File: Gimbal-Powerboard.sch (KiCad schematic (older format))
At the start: 117 parts

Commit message: Replaced legacy LaunchXL headers with new LaunchXL header device in schematic
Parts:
- removed U?: TIVA_Header_Pins, symbol TIVA_Header_Pins
- added U3: LAUNCHXL-F28069M_Launchpad_J1, MRDT_Shields:LAUNCHXL-F28069M_Launchpad_Programmer_Side, symbol LAUNCHXL-F28069M_Launchpad_J1
- gave numbers to parts that had none: 116
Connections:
- net ASENSE: now also U3.A_B1 (J3_24)
- net BSENSE: now also U3.A_A2 (J3_25)
- net CSENSE: now also U3.A_B2 (J3_26)
- net DC_CAL: now also U3.P_51 (J2_12)
- net DE: now also U3.P_13 (J4_34)
- net EN_GATE: now also U3.P_50 (J2_13)
- net GND: now also U3.GND (J3_22)
- net INH_A: now also U3.P_0 (J4_40)
- net INH_B: now also U3.P_2 (J4_38)
- net INH_C: now also U3.P_4 (J4_36)
- net INL_A: now also U3.P_1 (J4_39)
- net INL_B: now also U3.P_3 (J4_37)
- net INL_C: now also U3.P_5 (J4_35)
- net NFAULT: now also U3.P_33 (J1_9)
- net NOCTW: now also U3.P_32 (J1_10)
- net NSCS: now also U3.P_19 (J2_19)
- net PVDDSENSE: now also U3.A_A7 (J3_23)
- net PWM_IN: now also U3.DAC2 (J4_31)
- net SCLK: now also U3.P_18 (J1_7)
- net SDI: now also U3.P_16 (J2_15)
- net SDO: now also U3.P_17 (J2_14)
- net SO1: now also U3.A_A0 (J3_27)
- net SO2: now also U3.A_B0 (J3_28)
- net UART_RX: now also U3.P_28 (J1_3)
- net UART_TX: now also U3.P_29 (J1_4)
- net VCC: now also U3.+3V3 (J1_1)

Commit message: Github Fix Commit
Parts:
- removed C7: C, symbol C
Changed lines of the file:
@@
 EESchema Schematic File Version 2
-LIBS:Gimbal-Powerboard-rescue
 LIBS:power
 LIBS:device
@@
 LIBS:contrib
 LIBS:valves
-LIBS:MRDT-Actives
-LIBS:MRDT-Connectors
-LIBS:MRDT-Devices
-LIBS:MRDT-Drill_Holes
-LIBS:MRDT-Headers
-LIBS:MRDT-ICs
-LIBS:MRDT-Passives
-LIBS:MRDT-Shields
-LIBS:MRDT-Silkscreens
-LIBS:MRDT-Switches
 LIBS:Gimbal-Powerboard-cache
 EELAYER 25 0
@@
 F 2 "" H 5288 4900 50  0001 C CNN
 F 3 "" H 5250 5050 50  0001 C CNN
-	1    5250 5050
-	1    0    0    -1
-$EndComp
-$Comp
-L C C7
-U 1 1 5A7F8D38
-P 5250 5050
-F 0 "C7" H 5275 5150 50  0000 L CNN
-F 1 "C" H 5275 4950 50  0000 L CNN
-F 2 "" H 5288 4900 50  0001 C CNN
-F 3 "" H 5250 5050 50  0001 C CNN

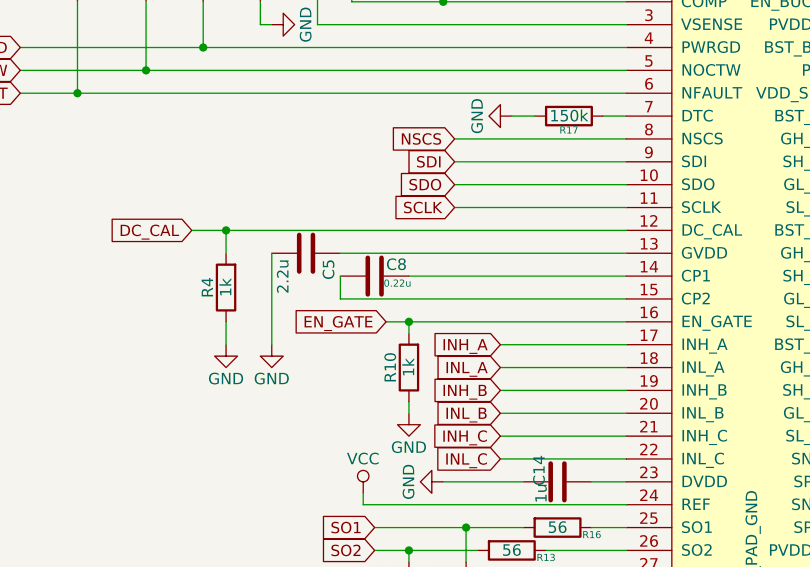
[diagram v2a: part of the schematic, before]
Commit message: Started device/package pairing
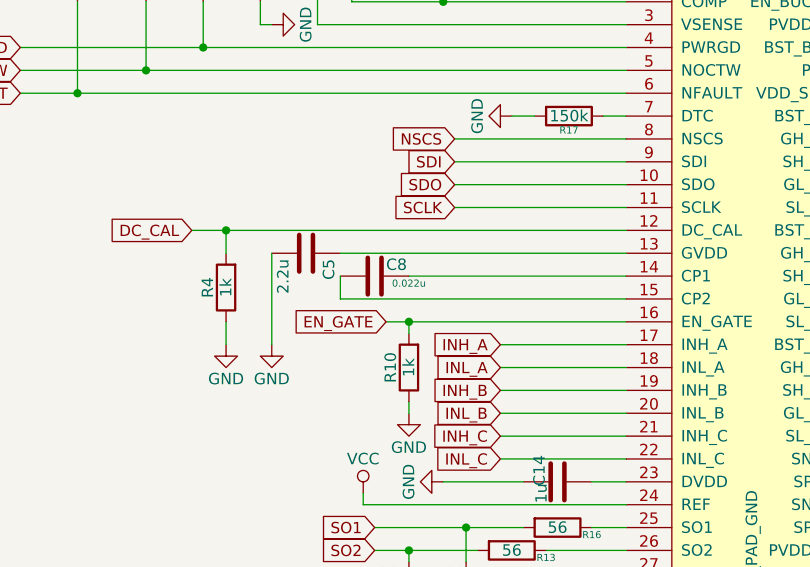
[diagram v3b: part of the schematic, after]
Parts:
- C1, C2: footprint (none) -> Capacitors_THT:CP_Radial_D12.5mm_P5.00mm
- C10, C11, C12, C13, C14, C15, C16, C17, C18, C20, C21, C23, C24, C25, C26, C27, C28, C3, C32, C33, C34, C35, C36, C4, C41, C42, C43, C6, C9: footprint (none) -> Capacitors_SMD:C_0805_HandSoldering
- C19, C22, C29, C30, C31, C5: footprint (none) -> Capacitors_SMD:C_1206_HandSoldering
- C8: value 0.22u -> 0.022u; footprint (none) -> Capacitors_SMD:C_0805_HandSoldering
- D1, D2, D3, D4: footprint (none) -> LEDs:LED_1206_HandSoldering
- D10, D11, D5, D6, D7, D8, D9: footprint (none) -> Diodes_SMD:D_SOD-323_HandSoldering

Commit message: Paired devices and packages for all components of schematic except MAX3232
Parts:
- C37: footprint (none) -> MRDT-Connectors:Anderson_2_Horisontal_Side-by-Side
- C38, C39, C40: footprint (none) -> MRDT-Connectors:Anderson_1_Horisontal
- L1: footprint (none) -> MRDT-Passives:DR74-330-R
- Q1, Q2: footprint (none) -> Diodes_SMD:D_SOT-23_ANK
- Q3, Q4, Q5, Q6, Q7, Q8: footprint (none) -> MRDT-Actives:Rohm_R6020ENJ_N-Channel_MOSFET
- R1, R10, R11, R12, R13, R14, R15, R16, R17, R18, R19, R2, R20, R21, R22, R23, R24, R25, R28, R29, R3, R30, R31, R32, R33, R4, R5, R6, R7, R8, R9: footprint (none) -> Resistors_SMD:R_0805_HandSoldering
- R26, R27: footprint (none) -> Resistors_SMD:R_1206_HandSoldering
- U1: footprint (none) -> MRDT-ICs:DRV8301
- U2: footprint (none) -> MRDT-ICs:NUP4201MR6
- U5: footprint (none) -> MRDT-Connectors:MOLEX_SL_3
- U6: footprint (none) -> MRDT-Connectors:MOLEX_SL_5

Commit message: Finished pairing devices with packages and generated netlist
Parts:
- TP1, TP10, TP11, TP12, TP13, TP14, TP15, TP2, TP3, TP4, TP5, TP6, TP7, TP8, TP9: footprint (none) -> Wire_Pads:SolderWirePad_single_1mmDrill
- U3: footprint MRDT_Shields:LAUNCHXL-F28069M_Launchpad_Programmer_Side -> MRDT_Shields:LAUNCHXL-F28069M_Launchpad_J1
- U4: footprint (none) -> MRDT_ICs:SOIC-16_3.9x9.9mm_Pitch1.27mm
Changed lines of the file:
@@
 F 0 "TP1" H 3800 3050 50  0000 C BNN
 F 1 "TEST" H 3800 3000 50  0000 C CNN
-F 2 "" H 3800 2750 50  0001 C CNN
+F 2 "Wire_Pads:SolderWirePad_single_1mmDrill" H 3800 2750 50  0001 C CNN
 F 3 "" H 3800 2750 50  0001 C CNN
 	1    3800 2750
@@
 F 0 "TP2" H 4350 5100 50  0000 C BNN
 F 1 "TEST" H 4350 5050 50  0000 C CNN
-F 2 "" H 4350 4800 50  0001 C CNN
+F 2 "Wire_Pads:SolderWirePad_single_1mmDrill" H 4350 4800 50  0001 C CNN
 F 3 "" H 4350 4800 50  0001 C CNN
 	1    4350 4800
@@
 F 0 "TP7" H 11950 3000 50  0000 C BNN
 F 1 "TEST" H 11950 2950 50  0000 C CNN
-F 2 "" H 11950 2700 50  0001 C CNN
+F 2 "Wire_Pads:SolderWirePad_single_1mmDrill" H 11950 2700 50  0001 C CNN
 F 3 "" H 11950 2700 50  0001 C CNN
 	1    11950 2700
@@
 F 0 "TP10" H 12950 3600 50  0000 C BNN
 F 1 "TEST" H 12950 3550 50  0000 C CNN
-F 2 "" H 12950 3300 50  0001 C CNN
+F 2 "Wire_Pads:SolderWirePad_single_1mmDrill" H 12950 3300 50  0001 C CNN
 F 3 "" H 12950 3300 50  0001 C CNN
 	1    12950 3300
@@
 F 0 "TP4" H 11800 3950 50  0000 C BNN
 F 1 "TEST" H 11800 3900 50  0000 C CNN
-F 2 "" H 11800 3650 50  0001 C CNN
+F 2 "Wire_Pads:SolderWirePad_single_1mmDrill" H 11800 3650 50  0001 C CNN
 F 3 "" H 11800 3650 50  0001 C CNN
 	1    11800 3650
@@
 F 0 "TP8" H 11950 6200 50  0000 C BNN
 F 1 "TEST" H 11950 6150 50  0000 C CNN
-F 2 "" H 11950 5900 50  0001 C CNN
+F 2 "Wire_Pads:SolderWirePad_single_1mmDrill" H 11950 5900 50  0001 C CNN
 F 3 "" H 11950 5900 50  0001 C CNN
 	1    11950 5900
@@
 F 0 "TP11" H 12950 6800 50  0000 C BNN
 F 1 "TEST" H 12950 6750 50  0000 C CNN
-F 2 "" H 12950 6500 50  0001 C CNN
+F 2 "Wire_Pads:SolderWirePad_single_1mmDrill" H 12950 6500 50  0001 C CNN
 F 3 "" H 12950 6500 50  0001 C CNN
 	1    12950 6500
@@
 F 0 "TP5" H 11800 7150 50  0000 C BNN
 F 1 "TEST" H 11800 7100 50  0000 C CNN
-F 2 "" H 11800 6850 50  0001 C CNN
+F 2 "Wire_Pads:SolderWirePad_single_1mmDrill" H 11800 6850 50  0001 C CNN
 F 3 "" H 11800 6850 50  0001 C CNN
 	1    11800 6850
@@
 F 0 "TP6" H 11900 9400 50  0000 C BNN
 F 1 "TEST" H 11900 9350 50  0000 C CNN
-F 2 "" H 11900 9100 50  0001 C CNN
+F 2 "Wire_Pads:SolderWirePad_single_1mmDrill" H 11900 9100 50  0001 C CNN
 F 3 "" H 11900 9100 50  0001 C CNN
 	1    11900 9100
@@
 F 0 "TP9" H 12900 10000 50  0000 C BNN
 F 1 "TEST" H 12900 9950 50  0000 C CNN
-F 2 "" H 12900 9700 50  0001 C CNN
+F 2 "Wire_Pads:SolderWirePad_single_1mmDrill" H 12900 9700 50  0001 C CNN
 F 3 "" H 12900 9700 50  0001 C CNN
 	1    12900 9700
@@
 F 0 "TP3" H 11750 10350 50  0000 C BNN
 F 1 "TEST" H 11750 10300 50  0000 C CNN
-F 2 "" H 11750 10050 50  0001 C CNN
+F 2 "Wire_Pads:SolderWirePad_single_1mmDrill" H 11750 10050 50  0001 C CNN
 F 3 "" H 11750 10050 50  0001 C CNN
 	1    11750 10050
@@
 F 0 "U4" H 17050 11025 50  0000 R CNN
 F 1 "MAX3232" H 17050 10950 50  0000 R CNN
-F 2 "" H 17200 8850 50  0001 L CNN
+F 2 "MRDT_ICs:SOIC-16_3.9x9.9mm_Pitch1.27mm" H 17200 8850 50  0001 L CNN
 F 3 "" H 17150 10000 50  0001 C CNN
 	1    17150 9900
@@
 F 0 "TP12" H 18050 5450 50  0000 C BNN
 F 1 "TEST" H 18050 5400 50  0000 C CNN
-F 2 "" H 18050 5150 50  0001 C CNN
+F 2 "Wire_Pads:SolderWirePad_single_1mmDrill" H 18050 5150 50  0001 C CNN
 F 3 "" H 18050 5150 50  0001 C CNN
 	1    18050 5150
@@
 F 0 "TP13" H 18200 5450 50  0000 C BNN
 F 1 "TEST" H 18200 5400 50  0000 C CNN
-F 2 "" H 18200 5150 50  0001 C CNN
+F 2 "Wire_Pads:SolderWirePad_single_1mmDrill" H 18200 5150 50  0001 C CNN
 F 3 "" H 18200 5150 50  0001 C CNN
 	1    18200 5150
@@
 F 0 "TP14" H 18350 5450 50  0000 C BNN
 F 1 "TEST" H 18350 5400 50  0000 C CNN
-F 2 "" H 18350 5150 50  0001 C CNN
+F 2 "Wire_Pads:SolderWirePad_single_1mmDrill" H 18350 5150 50  0001 C CNN
 F 3 "" H 18350 5150 50  0001 C CNN
 	1    18350 5150
@@
 F 0 "TP15" H 18500 5450 50  0000 C BNN
 F 1 "TEST" H 18500 5400 50  0000 C CNN
-F 2 "" H 18500 5150 50  0001 C CNN
+F 2 "Wire_Pads:SolderWirePad_single_1mmDrill" H 18500 5150 50  0001 C CNN
 F 3 "" H 18500 5150 50  0001 C CNN
 	1    18500 5150
@@
 F 0 "U3" H 16050 6500 60  0001 C CNN
 F 1 "LAUNCHXL-F28069M_Launchpad_J1" H 16200 7850 60  0000 C CNN
-F 2 "MRDT_Shields:LAUNCHXL-F28069M_Launchpad_Programmer_Side" H 15950 6550 60  0001 C CNN
+F 2 "MRDT_Shields:LAUNCHXL-F28069M_Launchpad_J1" H 15950 6550 60  0001 C CNN
 F 3 "" H 15950 6550 60  0001 C CNN
 	1    15950 5300

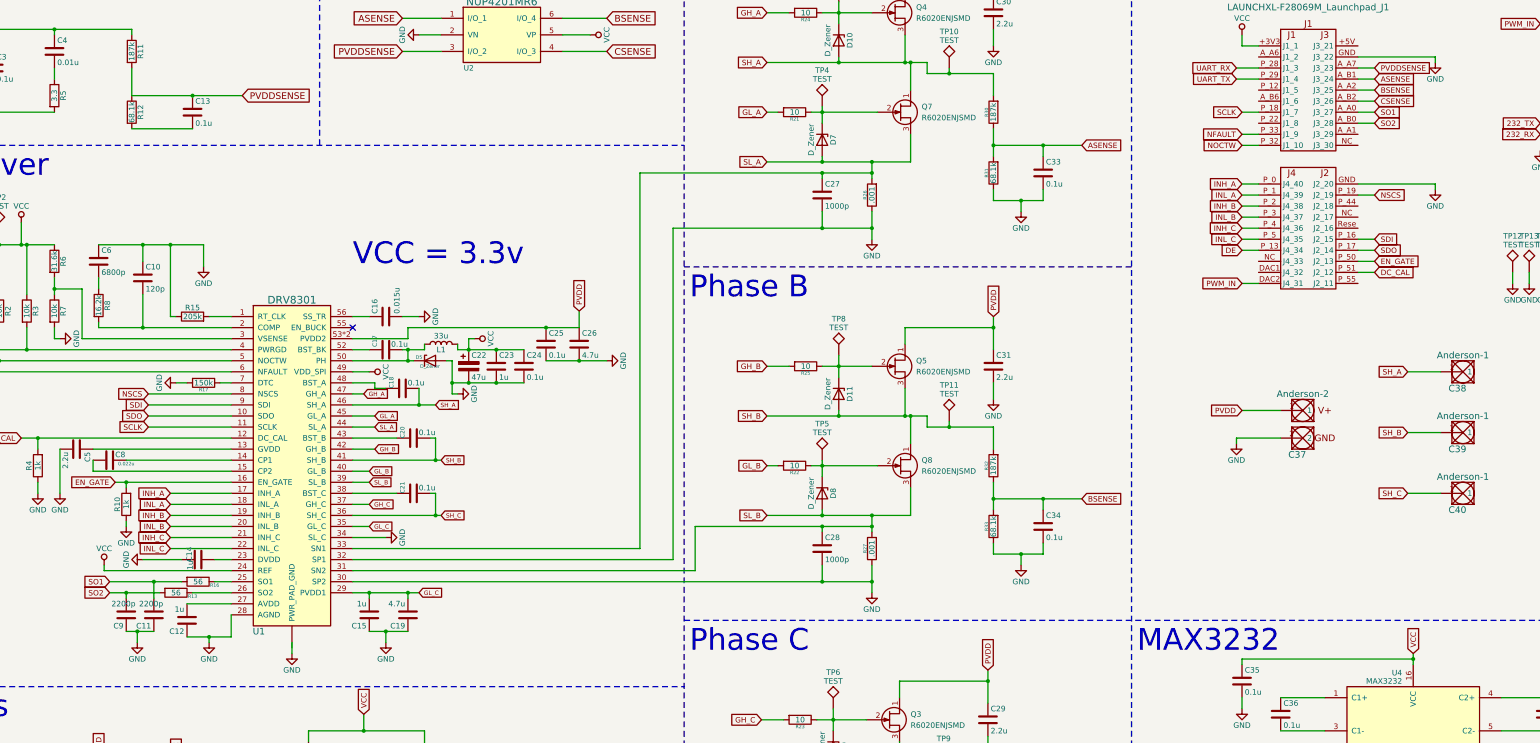
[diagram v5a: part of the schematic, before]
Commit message: Added preliminary adjustments for current sensor implementation
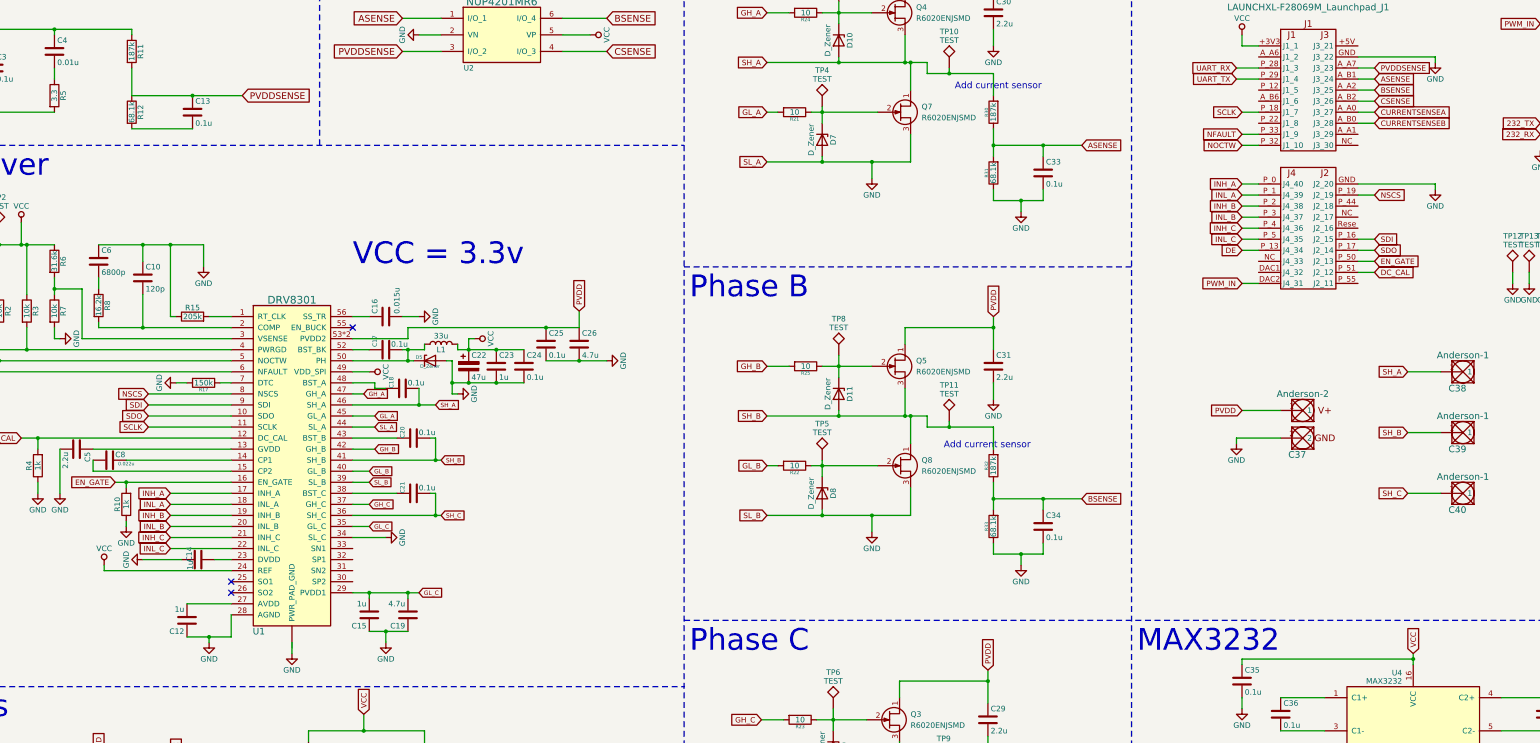
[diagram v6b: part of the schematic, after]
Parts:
- removed C11, C9: 2200p, Capacitors_SMD:C_0805_HandSoldering, symbol C
- removed C27, C28: 1000p, Capacitors_SMD:C_0805_HandSoldering, symbol C
- removed R13, R16: 56, Resistors_SMD:R_0805_HandSoldering, symbol R
- removed R26, R27: .001, Resistors_SMD:R_1206_HandSoldering, symbol R
- U3: footprint MRDT_Shields:LAUNCHXL-F28069M_Launchpad_J1 -> MRDT-Shields:LAUNCHXL-F28069M_Launchpad_J1
- U4: footprint MRDT_ICs:SOIC-16_3.9x9.9mm_Pitch1.27mm -> MRDT-ICs:SOIC-16_3.9x9.9mm_Pitch1.27mm
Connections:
- net GND: now also D7.2 (A), D8.2 (A), Q7.3 (S), Q8.3 (S), U1.39 (SL_B), U1.44 (SL_A); no longer U1.30 (SP2), U1.32 (SP1)
- removed net SL_A: D7.2 (A), Q7.3 (S), U1.33 (SN1), U1.44 (SL_A)
- removed net SL_B: D8.2 (A), Q8.3 (S), U1.31 (SN2), U1.39 (SL_B)
- net SO1 renamed CURRENTSENSEA
- net SO2 renamed CURRENTSENSEB
- no-connect marks 1 -> 3
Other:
- note added: "Add current sensor"
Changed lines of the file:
@@
-$EndComp
-$Comp
-L R R16
-U 1 1 5A801FB0
-P 6150 7950
-F 0 "R16" V 6200 8100 31  0000 C BNN
-F 1 "56" V 6150 7950 50  0000 C CNN
-F 2 "Resistors_SMD:R_0805_HandSoldering" V 6080 7950 50  0001 C CNN
-F 3 "" H 6150 7950 50  0001 C CNN
-	1    6150 7950
-	0    1    1    0
-$EndComp
-Text GLabel 5350 7950 0    49   Input ~ 0
-SO1
-$Comp
-L R R13
-U 1 1 5A802091
-P 5950 8050
-F 0 "R13" V 6000 8200 31  0000 C BNN
-F 1 "56" V 5950 8050 50  0000 C CNN
-F 2 "Resistors_SMD:R_0805_HandSoldering" V 5880 8050 50  0001 C CNN
-F 3 "" H 5950 8050 50  0001 C CNN
-	1    5950 8050
-	0    1    1    0
-$EndComp
-Text GLabel 5350 8050 0    49   Input ~ 0
-SO2
-$Comp
-L C C9
-U 1 1 5A80255D
-P 5500 8250
-F 0 "C9" H 5525 8350 50  0000 L CNN
-F 1 "2200p" H 5525 8150 50  0000 C CNN
-F 2 "Capacitors_SMD:C_0805_HandSoldering" H 5538 8100 50  0001 C CNN
-F 3 "" H 5500 8250 50  0001 C CNN
-	1    5500 8250
-	-1   0    0    1
-$EndComp
-$Comp
-L C C11
-U 1 1 5A802606
-P 5750 8250
-F 0 "C11" H 5775 8350 50  0000 L CNN
-F 1 "2200p" H 5775 8150 50  0000 C CNN
-F 2 "Capacitors_SMD:C_0805_HandSoldering" H 5788 8100 50  0001 C CNN
-F 3 "" H 5750 8250 50  0001 C CNN
-	1    5750 8250
-	-1   0    0    1
 $EndComp
 $Comp
@@
 $EndComp
 $Comp
-L GND #PWR013
-U 1 1 5A803150
-P 5600 8500
-F 0 "#PWR013" H 5600 8250 50  0001 C CNN
-F 1 "GND" H 5600 8350 50  0000 C CNN
-F 2 "" H 5600 8500 50  0001 C CNN
-F 3 "" H 5600 8500 50  0001 C CNN
-	1    5600 8500
-	1    0    0    -1
-$EndComp
-$Comp
 L C C16
 U 1 1 5A804E03
@@
 	0    1    1    0
 $EndComp
-$Comp
-L R R26
-U 1 1 5A80D189
-P 12250 4450
-F 0 "R26" V 12330 4450 31  0000 C BNN
-F 1 ".001" V 12250 4450 50  0000 C CNN
-F 2 "Resistors_SMD:R_1206_HandSoldering" V 12180 4450 50  0001 C CNN
-F 3 "" H 12250 4450 50  0001 C CNN
-	1    12250 4450
-	-1   0    0    1
-$EndComp
 Text GLabel 11300 4150 0    49   Input ~ 0
 SL_A
-$Comp
-L C C27
-U 1 1 5A80DD57
-P 11800 4450
-F 0 "C27" H 11825 4550 50  0000 L CNN
-F 1 "1000p" H 11825 4350 50  0000 L CNN
-F 2 "Capacitors_SMD:C_0805_HandSoldering" H 11838 4300 50  0001 C CNN
-F 3 "" H 11800 4450 50  0001 C CNN
-	1    11800 4450
-	1    0    0    -1
-$EndComp
-$Comp
-L GND #PWR024
-U 1 1 5A80FE41
-P 12250 4850
-F 0 "#PWR024" H 12250 4600 50  0001 C CNN
-F 1 "GND" H 12250 4700 50  0000 C CNN
-F 2 "" H 12250 4850 50  0001 C CNN
-F 3 "" H 12250 4850 50  0001 C CNN
-	1    12250 4850
-	1    0    0    -1
-$EndComp
 Text Notes 10600 5400 0    197  ~ 0
 Phase B
@@
 	0    1    1    0
 $EndComp
-$Comp
-L R R27
-U 1 1 5A8193BC
-P 12250 7650
-F 0 "R27" V 12330 7650 31  0000 C BNN
-F 1 ".001" V 12250 7650 50  0000 C CNN
-F 2 "Resistors_SMD:R_1206_HandSoldering" V 12180 7650 50  0001 C CNN
-F 3 "" H 12250 7650 50  0001 C CNN
-	1    12250 7650
-	-1   0    0    1
-$EndComp
 Text GLabel 11300 7350 0    49   Input ~ 0
 SL_B
 $Comp
-L C C28
-U 1 1 5A8193C3
-P 11800 7650
-F 0 "C28" H 11825 7750 50  0000 L CNN
-F 1 "1000p" H 11825 7550 50  0000 L CNN
-F 2 "Capacitors_SMD:C_0805_HandSoldering" H 11838 7500 50  0001 C CNN
-F 3 "" H 11800 7650 50  0001 C CNN
-	1    11800 7650
-	1    0    0    -1
-$EndComp
-$Comp
 L GND #PWR027
 U 1 1 5A8193C9
-P 12250 8050
-F 0 "#PWR027" H 12250 7800 50  0001 C CNN
-F 1 "GND" H 12250 7900 50  0000 C CNN
-F 2 "" H 12250 8050 50  0001 C CNN
-F 3 "" H 12250 8050 50  0001 C CNN
-	1    12250 8050
+P 12250 7500
+F 0 "#PWR027" H 12250 7250 50  0001 C CNN
+F 1 "GND" H 12250 7350 50  0000 C CNN
+F 2 "" H 12250 7500 50  0001 C CNN
+F 3 "" H 12250 7500 50  0001 C CNN
+	1    12250 7500
 	1    0    0    -1
 $EndComp
@@
 F 0 "U4" H 17050 11025 50  0000 R CNN
 F 1 "MAX3232" H 17050 10950 50  0000 R CNN
-F 2 "MRDT_ICs:SOIC-16_3.9x9.9mm_Pitch1.27mm" H 17200 8850 50  0001 L CNN
+F 2 "MRDT-ICs:SOIC-16_3.9x9.9mm_Pitch1.27mm" H 17200 8850 50  0001 L CNN
 F 3 "" H 17150 10000 50  0001 C CNN
 	1    17150 9900
@@
 F 0 "U3" H 16050 6500 60  0001 C CNN
 F 1 "LAUNCHXL-F28069M_Launchpad_J1" H 16200 7850 60  0000 C CNN
-F 2 "MRDT_Shields:LAUNCHXL-F28069M_Launchpad_J1" H 15950 6550 60  0001 C CNN
+F 2 "MRDT-Shields:LAUNCHXL-F28069M_Launchpad_J1" H 15950 6550 60  0001 C CNN
 F 3 "" H 15950 6550 60  0001 C CNN
 	1    15950 5300
@@
 DE
 Text GLabel 16800 3700 2    49   Input ~ 0
-SO1
+CURRENTSENSEA
 Text GLabel 16800 3800 2    49   Input ~ 0
-SO2
+CURRENTSENSEB
 $Comp
 L VCC #PWR046
@@
 	11250 9200 11450 9200
 Wire Wire Line
-	11800 4250 11800 4300
-Wire Wire Line
 	11800 4100 11800 4150
-Connection ~ 12250 4750
-Connection ~ 11800 4750
-Connection ~ 12250 4250
-Connection ~ 11800 4250
-Wire Wire Line
-	12250 4600 12250 4850
-Wire Wire Line
-	11800 4600 11800 4750
-Wire Wire Line
-	12250 4150 12250 4300
 Wire Wire Line
 	11800 3650 11800 3800
 Connection ~ 11800 4150
-Connection ~ 12250 4150
 Wire Wire Line
 	11300 4150 12600 4150
@@
 Wire Wire Line
 	7550 5550 7700 5550
-Connection ~ 5600 8400
-Wire Wire Line
-	5600 8500 5600 8400
-Wire Wire Line
-	5500 8400 5750 8400
 Connection ~ 6250 8450
 Wire Wire Line
@@
 Wire Wire Line
 	6050 8150 6450 8150
-Connection ~ 5500 8050
-Wire Wire Line
-	5500 8050 5500 8100
-Connection ~ 5750 7950
-Wire Wire Line
-	5750 7950 5750 8100
-Wire Wire Line
-	6100 8050 6450 8050
-Wire Wire Line
-	5350 8050 5800 8050
-Wire Wire Line
-	6000 7950 5350 7950
-Wire Wire Line
-	6450 7950 6300 7950
 Wire Wire Line
 	5300 7800 5300 7850
@@
 	3050 8900 10550 8900
 Wire Wire Line
-	11800 7450 11800 7500
-Wire Wire Line
 	11800 7300 11800 7350
-Connection ~ 12250 7950
-Connection ~ 11800 7950
-Connection ~ 12250 7450
-Connection ~ 11800 7450
-Wire Wire Line
-	12250 7800 12250 8050
-Wire Wire Line
-	11800 7800 11800 7950
-Wire Wire Line
-	12250 7350 12250 7500
 Wire Wire Line
 	11800 6850 11800 7000
@@
 Wire Notes Line
 	3050 11400 19700 11400
-Wire Wire Line
-	10150 4250 12250 4250
-Wire Wire Line
-	10150 4250 10150 7650
-Wire Wire Line
-	10150 7650 7550 7650
-Wire Wire Line
-	10450 4750 12250 4750
-Wire Wire Line
-	10450 4750 10450 7750
-Wire Wire Line
-	10450 7750 7550 7750
-Wire Wire Line
-	10650 7450 12250 7450
-Wire Wire Line
-	10650 7450 10650 7850
-Wire Wire Line
-	10650 7850 7550 7850
-Wire Wire Line
-	7550 7950 12250 7950
 Wire Wire Line
 	18300 2900 18600 2900
@@
 Wire Wire Line
 	15550 3300 15750 3300
+Wire Wire Line
+	12250 7500 12250 7350
+Connection ~ 12250 4150
+Wire Wire Line
+	12250 4300 12250 4150
+$Comp
+L GND #PWR024
+U 1 1 5A80FE41
+P 12250 4300
+F 0 "#PWR024" H 12250 4050 50  0001 C CNN
+F 1 "GND" H 12250 4150 50  0000 C CNN
+F 2 "" H 12250 4300 50  0001 C CNN
+F 3 "" H 12250 4300 50  0001 C CNN
+	1    12250 4300
+	1    0    0    -1
+$EndComp
+NoConn ~ 6450 7950
+NoConn ~ 6450 8050
+Text Notes 13000 3500 0    60   ~ 0
+Add current sensor
+Text Notes 12900 6750 0    60   ~ 0
+Add current sensor
 $EndSCHEMATC
